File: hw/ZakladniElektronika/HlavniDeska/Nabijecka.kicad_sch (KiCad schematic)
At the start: 1 part

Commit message: WIP
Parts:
- added C146, C147: 47n, Capacitor_SMD:C_0402_1005Metric, symbol Device:C
- added D126: red, LED_SMD:LED_0603_1608Metric, symbol Device:LED
- added L5: 1u, Robotarna_KiCad_Library:SMD,4.2x4.4mm, symbol Device:L
- added R13: 4.7k, Resistor_SMD:R_0201_0603Metric, symbol Device:R
- added R13: 200k, Resistor_SMD:R_0402_1005Metric, symbol Device:R
- added R13: 10k, Resistor_SMD:R_0402_1005Metric, symbol Device:R
- added R13: 3k, Resistor_SMD:R_0402_1005Metric, symbol Device:R
- added R13: 47k, Resistor_SMD:R_0402_1005Metric, symbol Device:R
- added R13: 15k, Resistor_SMD:R_0402_1005Metric, symbol Device:R
- added R22, R23: 100, Resistor_SMD:R_0402_1005Metric, symbol Device:R
- added U5 (x12): 10uf, Capacitor_SMD:C_0805_2012Metric, symbol B.B-rescue:C-Device-B.B-rescue-B.B-rescue
- added U5: 1n, Capacitor_SMD:C_0402_1005Metric, symbol B.B-rescue:C-Device-B.B-rescue-B.B-rescue
- added U6 (x3): 100n, Capacitor_SMD:C_0402_1005Metric, symbol B.B-rescue:C-Device-B.B-rescue-B.B-rescue
- U35: value ~ -> BQ24179
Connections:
- net GMD: now also U35.G2 (ACDRV2), U35.H2 (ACDRV1), R13.1, R13.1, R13.1, R23.2, U5.2, U5.2, U5.2, U5.2, U5.2, U5.2, U5.2, U5.2, U5.2, U5.2, U5.2, U5.2, U5.2, U6.2, U6.2, U6.2
- net PMID: now also U5.1, U5.1, U5.1, U6.1
- net SW1: now also C147.1, L5.2
- net SW2: now also C146.1, L5.1
- net VBUS: now also U35.G1 (VAC2), U35.H1 (VAC1), U5.1, U5.1, U6.1
- net at U35.A6 (SYS), U35.B6 (SYS), U35.C6 (SYS)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: now also U5.1, U5.1, U5.1, U5.1, U5.1, U6.1
- net BAT: now reaches U35.A7 (BAT), U35.B7 (BAT), U35.C7 (BAT), U35.D7 (BAT), U35.E7 (BAT)
- net BAT: now also R22.2, U5.1, U5.1
- net at U35.D1 (BTST1): now also C147.2
- net at U35.E1 (REGN): now also R13.1
- net at U35.F1 (STAT): now also D126.2 (A)
- net D+: now reaches U35.F2 (D+)
- net D-: now reaches U35.F3 (D-)
- net at U35.F4 (ILIM_HIZ): now also R13.2
- net at U35.F5 (PROG): now also R13.2
- net at U35.F6 (SDRV): now also U5.1
- net at U35.F7 (BTST2): now also C146.2
- net QON: now reaches U35.G3 (QON)
- net CE: now reaches U35.G4 (CE)
- net INT: now reaches U35.G5 (INT)
- net at U35.G6 (BATN): now also R23.1
- net at U35.G7 (BATP): now also R22.1
- net SCL: now reaches U35.H4 (SCL)
- net SDA: now reaches U35.H5 (SDA)
- net at U35.H7 (TS): now also R13.2
- new net: D126.1 (K), R13.2
- new net: R13.1, R13.2 (x2)
- no-connect marks 0 -> 2
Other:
- moved on the sheet: U35

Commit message: Zaciame psat
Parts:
- U35: LCSC (none) -> C2879484
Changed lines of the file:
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@@
       (effects (font (size 1.27 1.27)) hide)
     )
-    (property "Datasheet" "" (at 133.35 50.8 0)
+    (property "Datasheet" "https://www.ti.com/lit/ds/symlink/bq24179.pdf?ts=1698854511988&ref_url=https%253A%252F%252Fwww.ti.com%252Fpower-management%252Fbattery-management%252Fcharger-ics%252Fproducts.html" (at 133.35 50.8 0)
       (effects (font (size 1.27 1.27)) hide)
     )
+    (property "LCSC" "C2879484" (at 133.35 50.8 0)
+      (effects (font (size 1.27 1.27)) hide)
+    )

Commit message: USB_multiplexer a přehlednost
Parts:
- removed C146, C147: 47n, Capacitor_SMD:C_0402_1005Metric, symbol Device:C
- removed L5: 1u, Robotarna_KiCad_Library:SMD,4.2x4.4mm, symbol Device:L
- removed R13: 4.7k, Resistor_SMD:R_0201_0603Metric, symbol Device:R
- removed R13: 200k, Resistor_SMD:R_0402_1005Metric, symbol Device:R
- removed R13: 10k, Resistor_SMD:R_0402_1005Metric, symbol Device:R
- removed R13: 3k, Resistor_SMD:R_0402_1005Metric, symbol Device:R
- removed R13: 47k, Resistor_SMD:R_0402_1005Metric, symbol Device:R
- removed R13: 15k, Resistor_SMD:R_0402_1005Metric, symbol Device:R
- removed R22, R23: 100, Resistor_SMD:R_0402_1005Metric, symbol Device:R
- removed U35: BQ24179, symbol Robotarna_KiCad_Library:BQ24179
- removed U5 (x12): 10uf, Capacitor_SMD:C_0805_2012Metric, symbol B.B-rescue:C-Device-B.B-rescue-B.B-rescue
- removed U5: 1n, Capacitor_SMD:C_0402_1005Metric, symbol B.B-rescue:C-Device-B.B-rescue-B.B-rescue
- removed U6 (x3): 100n, Capacitor_SMD:C_0402_1005Metric, symbol B.B-rescue:C-Device-B.B-rescue-B.B-rescue
- added C150: 4.7u, Capacitor_SMD:C_0805_2012Metric, symbol Device:C
- added C165: 47n, Capacitor_SMD:C_0402_1005Metric, symbol Device:C
- added C3: 1u, Capacitor_SMD:C_0402_1005Metric, symbol Device:C
- added L7: L, Inductor_SMD:L_Abracon_ASPI-0630LR, symbol Device:L
- added R13: 4.7k, Resistor_SMD:R_0201_0603Metric, symbol Device:R
- added R13 (x2): 10k, Resistor_SMD:R_0402_1005Metric, symbol Device:R
- added R17 (x2): 0, Resistor_SMD:R_0805_2012Metric_Pad1.20x1.40mm_HandSolder, symbol Device:R
- added R72: 100, Resistor_SMD:R_0402_1005Metric, symbol Device:R
- added TP4: TestPoint-Charger_QON, symbol Connector:TestPoint
- added TP4: TestPoint-Charger_ILIM, symbol Connector:TestPoint
- added U5 (x3): 10uf, Capacitor_SMD:C_0805_2012Metric, symbol B.B-rescue:C-Device-B.B-rescue-B.B-rescue
- added U9: BQ25895RTW, Package_DFN_QFN:Texas_S-PWQFN-N24_EP2.7x2.7mm_ThermalVias, symbol Battery_Management:BQ25895RTW
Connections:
- net D+: now also U9.2 (D+)
- net D-: now also U9.3 (D-)
- net INT: now also U9.7 (INT)
- net SCL: now also U9.5 (SCL)
- net SDA: now also U9.6 (SDA)
- net VBUS: now also C3.1, U9.1 (VBUS)
- net at D126.1 (K): now also R13.2
- net at D126.2 (A): now also U9.13 (BAT), U9.14 (BAT)
- new net: U5.1, U9.23 (PMID)
- new net: C165.1, L7.1, U9.19 (SW), U9.20 (SW)
- new net: C165.2, U9.21 (BTST)
- new net: C150.1, R13.2, U9.22 (REGN)
- new net: L7.2, U5.1, U5.1, U9.15 (SYS), U9.16 (SYS)
- new net: TP4.1, U9.12 (~{QON})
- new net: R17.2, U9.8 (OTG)
- new net: R17.2, U9.9 (~{CE})
- new net: R72.1, TP4.1, U9.10 (ILIM)
- new net: R13.1, U9.4 (STAT)
- new net: R13.1, R13.1, U9.11 (TS)
- new net DSEL: U9.24 (DSEL)
- new net GND: C150.2, C3.2, R13.2, R17.1, R17.1, R72.2, U5.2, U5.2, U5.2, U9.17 (PGND), U9.18 (PGND), U9.25 (PGND)
- no-connect marks 2 -> 0

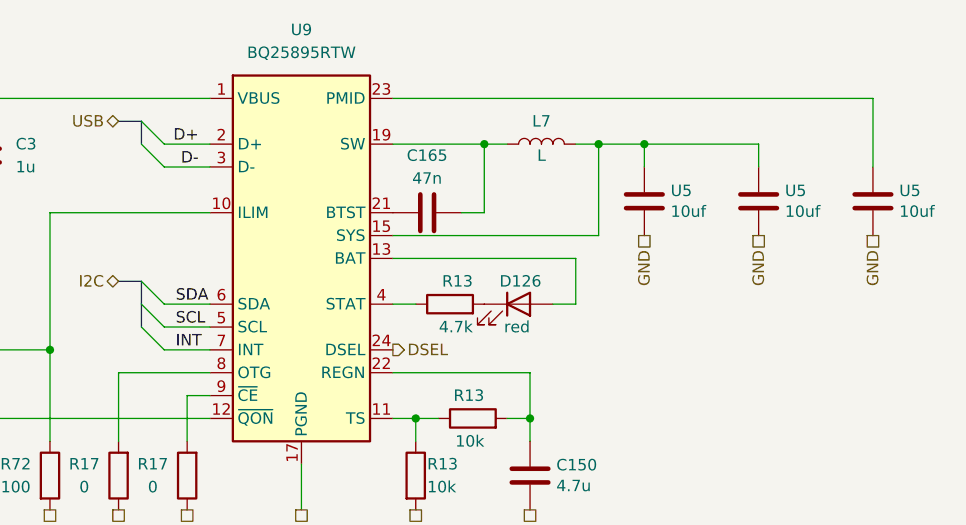
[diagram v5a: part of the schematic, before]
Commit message: Likvidace MiniUI jako samostatné desky a výběr všech komponent
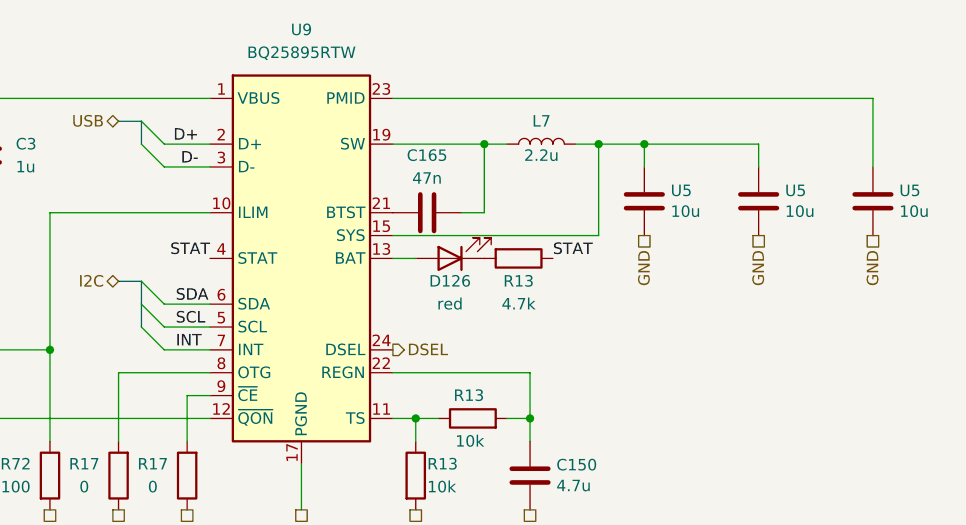
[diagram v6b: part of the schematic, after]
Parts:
- C150: footprint Capacitor_SMD:C_0805_2012Metric -> Capacitor_SMD:C_0603_1608Metric; Basic/Extended (none) -> B; LCSC C1779 -> C19666; info (none) -> 16V, X5R
- C165: footprint Capacitor_SMD:C_0402_1005Metric -> Capacitor_SMD:C_0603_1608Metric; Basic/Extended (none) -> B; LCSC (none) -> C1622; info (none) -> 50V, X7R
- C3: JLCPCB_CORRECTION (none) -> 0;0;0; info 50V, X7R -> 50V, X5R (potenciálně C52923 což je 25V, X5R )
- L7: value L -> 2.2u; Basic/Extended (none) -> E
- R13: footprint Resistor_SMD:R_0201_0603Metric -> Resistor_SMD:R_0402_1005Metric; Basic/Extended E -> B; LCSC C270346 -> C25900
- R13: JLCPCB_CORRECTION (none) -> 0;0;0
- R17: Basic/Extended (none) -> B; LCSC C908865 -> C17477
- R72: Basic/Extended (none) -> B
- TP4: JLCPCB_IGNORE (none) -> ignore
- U5: value 10uf -> 10u; footprint Capacitor_SMD:C_0805_2012Metric -> Capacitor_SMD:C_0603_1608Metric; Basic/Extended (none) -> B; LCSC C15850 -> C96446; info (none) -> 25V, X5R
- U9: Basic/Extended (none) -> E; LCSC (none) -> C80200
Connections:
- net STAT: now reaches R13.1, U9.4 (STAT)
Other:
- moved on the sheet: D126, R13

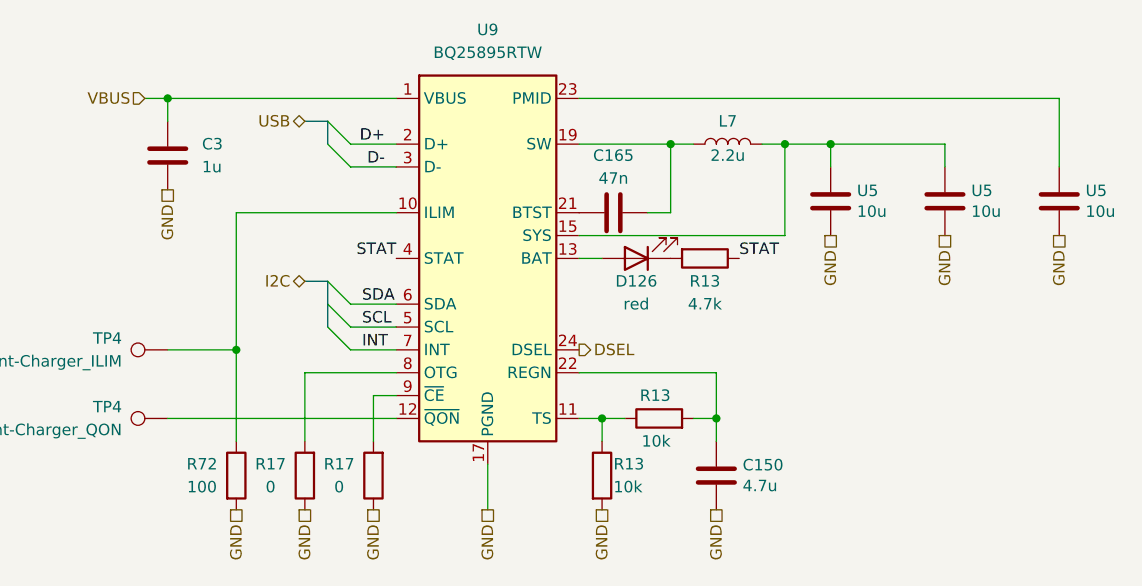
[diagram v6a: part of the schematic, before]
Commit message: Výmněna ochrany baterie
Předchozí ochranný čip JLCPCB nemělo na skladě
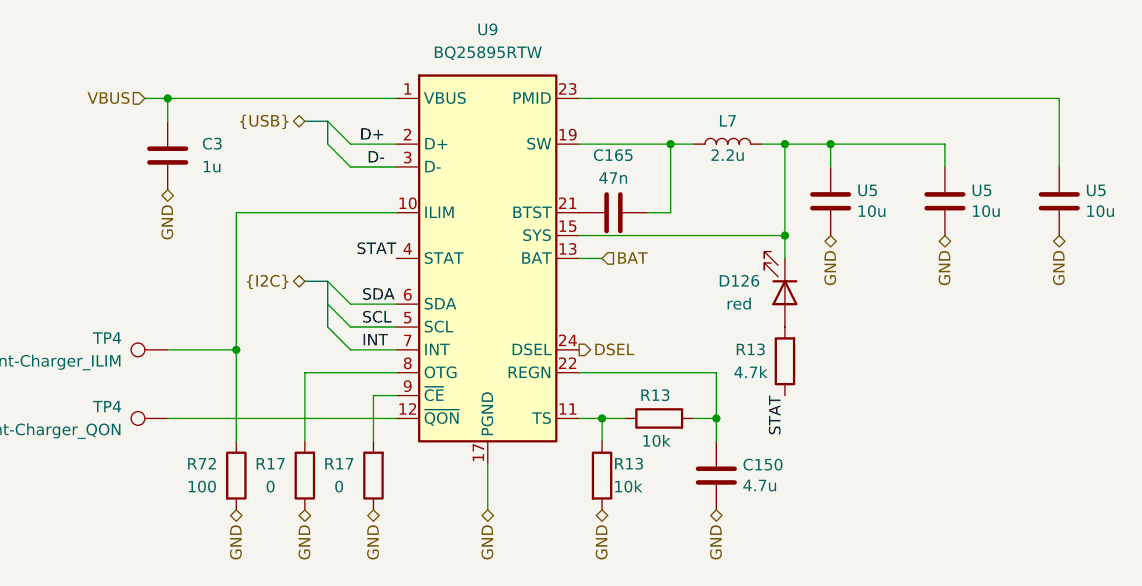
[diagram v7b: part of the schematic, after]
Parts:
- TP4: footprint (none) -> Connector_Pin:Pin_D0.9mm_L10.0mm_W2.4mm_FlatFork
- U5: symbol B.B-rescue:C-Device-B.B-rescue-B.B-rescue -> Device:C
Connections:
- net at L7.2, U5.1, U5.1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: now also D126.1 (K)
- net at R13.2: now also D126.2 (A); no longer D126.1 (K)
- net BAT: now reaches U9.13 (BAT), U9.14 (BAT)
- net BAT: no longer D126.2 (A)
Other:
- moved on the sheet: D126, R13
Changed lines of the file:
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@@
   (junction (at 109.22 91.44) (diameter 0) (color 0 0 0 0)
   )
+  (junction (at 170.18 78.74) (diameter 0) (color 0 0 0 0)
+  )
   (junction (at 101.6 63.5) (diameter 0) (color 0 0 0 0)
   )
@@
   )
   (wire (pts (xy 170.18 78.74) (xy 170.18 68.58))
+    (stroke (width 0) (type default))
+  )
+  (wire (pts (xy 170.18 78.74) (xy 170.18 81.28))
     (stroke (width 0) (type default))
   )
@@
     (effects (font (size 1.27 1.27)) (justify left bottom))
   )
-  (label "STAT" (at 165.1 81.28 0) (fields_autoplaced)
-    (effects (font (size 1.27 1.27)) (justify left bottom))
+  (label "STAT" (at 170.18 96.52 270) (fields_autoplaced)
+    (effects (font (size 1.27 1.27)) (justify right bottom))
   )
   (hierarchical_label "VBUS" (shape input) (at 99.06 63.5 180) (fields_autoplaced)
@@
     (effects (font (size 1.27 1.27)) (justify left))
   )
-  (hierarchical_label "GND" (shape passive) (at 109.22 109.22 270) (fields_autoplaced)
-    (effects (font (size 1.27 1.27)) (justify right))
-  )
-  (hierarchical_label "GND" (shape passive) (at 187.96 78.74 270) (fields_autoplaced)
-    (effects (font (size 1.27 1.27)) (justify right))
-  )
-  (hierarchical_label "GND" (shape passive) (at 101.6 73.66 270) (fields_autoplaced)
-    (effects (font (size 1.27 1.27)) (justify right))
-  )
-  (hierarchical_label "GND" (shape passive) (at 162.56 109.22 270) (fields_autoplaced)
-    (effects (font (size 1.27 1.27)) (justify right))
-  )
-  (hierarchical_label "I2C" (shape bidirectional) (at 116.84 83.82 180) (fields_autoplaced)
-    (effects (font (size 1.27 1.27)) (justify right))
-  )
-  (hierarchical_label "USB" (shape bidirectional) (at 116.84 66.04 180) (fields_autoplaced)
-    (effects (font (size 1.27 1.27)) (justify right))
-  )
-  (hierarchical_label "GND" (shape passive) (at 149.86 109.22 270) (fields_autoplaced)
-    (effects (font (size 1.27 1.27)) (justify right))
-  )
-  (hierarchical_label "GND" (shape passive) (at 175.26 78.74 270) (fields_autoplaced)
-    (effects (font (size 1.27 1.27)) (justify right))
-  )
-  (hierarchical_label "GND" (shape passive) (at 200.66 78.74 270) (fields_autoplaced)
-    (effects (font (size 1.27 1.27)) (justify right))
-  )
-  (hierarchical_label "GND" (shape passive) (at 124.46 109.22 270) (fields_autoplaced)
-    (effects (font (size 1.27 1.27)) (justify right))
-  )
-  (hierarchical_label "GND" (shape passive) (at 137.16 109.22 270) (fields_autoplaced)
-    (effects (font (size 1.27 1.27)) (justify right))
-  )
-  (hierarchical_label "GND" (shape passive) (at 116.84 109.22 270) (fields_autoplaced)
-    (effects (font (size 1.27 1.27)) (justify right))
-  )
-  (symbol (lib_id "B.B-rescue:C-Device-B.B-rescue-B.B-rescue") (at 200.66 74.93 0) (unit 1)
+  (hierarchical_label "BAT" (shape input) (at 149.86 81.28 0) (fields_autoplaced)
+    (effects (font (size 1.27 1.27)) (justify left))
+  )
+  (hierarchical_label "GND" (shape bidirectional) (at 109.22 109.22 270) (fields_autoplaced)
+    (effects (font (size 1.27 1.27)) (justify right))
+  )
+  (hierarchical_label "GND" (shape bidirectional) (at 187.96 78.74 270) (fields_autoplaced)
+    (effects (font (size 1.27 1.27)) (justify right))
+  )
+  (hierarchical_label "GND" (shape bidirectional) (at 101.6 73.66 270) (fields_autoplaced)
+    (effects (font (size 1.27 1.27)) (justify right))
+  )
+  (hierarchical_label "GND" (shape bidirectional) (at 162.56 109.22 270) (fields_autoplaced)
+    (effects (font (size 1.27 1.27)) (justify right))
+  )
+  (hierarchical_label "{I2C}" (shape bidirectional) (at 116.84 83.82 180) (fields_autoplaced)
+    (effects (font (size 1.27 1.27)) (justify right))
+  )
+  (hierarchical_label "{USB}" (shape bidirectional) (at 116.84 66.04 180) (fields_autoplaced)
+    (effects (font (size 1.27 1.27)) (justify right))
+  )
+  (hierarchical_label "GND" (shape bidirectional) (at 149.86 109.22 270) (fields_autoplaced)
+    (effects (font (size 1.27 1.27)) (justify right))
+  )
+  (hierarchical_label "GND" (shape bidirectional) (at 175.26 78.74 270) (fields_autoplaced)
+    (effects (font (size 1.27 1.27)) (justify right))
+  )
+  (hierarchical_label "GND" (shape bidirectional) (at 200.66 78.74 270) (fields_autoplaced)
+    (effects (font (size 1.27 1.27)) (justify right))
+  )
+  (hierarchical_label "GND" (shape bidirectional) (at 124.46 109.22 270) (fields_autoplaced)
+    (effects (font (size 1.27 1.27)) (justify right))
+  )
+  (hierarchical_label "GND" (shape bidirectional) (at 137.16 109.22 270) (fields_autoplaced)
+    (effects (font (size 1.27 1.27)) (justify right))
+  )
+  (hierarchical_label "GND" (shape bidirectional) (at 116.84 109.22 270) (fields_autoplaced)
+    (effects (font (size 1.27 1.27)) (justify right))
+  )
+  (symbol (lib_id "Device:C") (at 200.66 74.93 0) (unit 1)
     (in_bom yes) (on_board yes) (dnp no)
     (property "Reference" "U5" (at 203.581 73.7616 0)
@@
     )
   )
-  (symbol (lib_id "B.B-rescue:C-Device-B.B-rescue-B.B-rescue") (at 187.96 74.93 0) (unit 1)
+  (symbol (lib_id "Device:C") (at 187.96 74.93 0) (unit 1)
     (in_bom yes) (on_board yes) (dnp no)
     (property "Reference" "U5" (at 190.881 73.7616 0)
@@
       (effects (font (size 1.27 1.27)) (justify left))
     )
-    (property "Footprint" "" (at 101.6 93.98 0)
+    (property "Footprint" "Connector_Pin:Pin_D0.9mm_L10.0mm_W2.4mm_FlatFork" (at 101.6 93.98 0)
       (effects (font (size 1.27 1.27)) hide)
     )
@@
       (effects (font (size 1.27 1.27)) (justify left))
     )
-    (property "Footprint" "" (at 101.6 86.36 0)
+    (property "Footprint" "Connector_Pin:Pin_D0.9mm_L10.0mm_W2.4mm_FlatFork" (at 101.6 86.36 0)
       (effects (font (size 1.27 1.27)) hide)
     )
@@
     )
   )
-  (symbol (lib_id "Device:R") (at 161.29 81.28 270) (unit 1)
-    (in_bom yes) (on_board yes) (dnp no)
-    (property "Reference" "R13" (at 161.29 83.82 90)
-      (effects (font (size 1.27 1.27)))
-    )
-    (property "Value" "4.7k" (at 161.29 86.36 90)
-      (effects (font (size 1.27 1.27)))
-    )
-    (property "Footprint" "Resistor_SMD:R_0402_1005Metric" (at 161.29 79.502 90)
-      (effects (font (size 1.27 1.27)) hide)
-    )
-    (property "Datasheet" "~" (at 161.29 81.28 0)
-      (effects (font (size 1.27 1.27)) hide)
-    )
-    (property "LCSC" "C25900" (at 161.29 81.28 0)
-      (effects (font (size 1.27 1.27)) hide)
-    )
-    (property "Basic/Extended" "B" (at 161.29 81.28 0)
+  (symbol (lib_id "Device:R") (at 170.18 92.71 180) (unit 1)
+    (in_bom yes) (on_board yes) (dnp no)
+    (property "Reference" "R13" (at 166.37 91.44 0)
+      (effects (font (size 1.27 1.27)))
+    )
+    (property "Value" "4.7k" (at 166.37 93.98 0)
+      (effects (font (size 1.27 1.27)))
+    )
+    (property "Footprint" "Resistor_SMD:R_0402_1005Metric" (at 171.958 92.71 90)
+      (effects (font (size 1.27 1.27)) hide)
+    )
+    (property "Datasheet" "~" (at 170.18 92.71 0)
+      (effects (font (size 1.27 1.27)) hide)
+    )
+    (property "LCSC" "C25900" (at 170.18 92.71 0)
+      (effects (font (size 1.27 1.27)) hide)
+    )
+    (property "Basic/Extended" "B" (at 170.18 92.71 0)
       (effects (font (size 1.27 1.27)) hide)
     )
@@
     )
   )
-  (symbol (lib_id "B.B-rescue:C-Device-B.B-rescue-B.B-rescue") (at 175.26 74.93 0) (unit 1)
+  (symbol (lib_id "Device:C") (at 175.26 74.93 0) (unit 1)
     (in_bom yes) (on_board yes) (dnp no)
     (property "Reference" "U5" (at 178.181 73.7616 0)
@@
     )
   )
-  (symbol (lib_id "Device:LED") (at 153.67 81.28 180) (unit 1)
-    (in_bom yes) (on_board yes) (dnp no)
-    (property "Reference" "D126" (at 153.67 83.82 0)
-      (effects (font (size 1.27 1.27)))
-    )
-    (property "Value" "red" (at 153.67 86.36 0)
-      (effects (font (size 1.27 1.27)))
-    )
-    (property "Footprint" "LED_SMD:LED_0603_1608Metric" (at 153.67 81.28 0)
-      (effects (font (size 1.27 1.27)) hide)
-    )
-    (property "Datasheet" "~" (at 153.67 81.28 0)
-      (effects (font (size 1.27 1.27)) hide)
-    )
-    (property "LCSC" "C2286" (at 153.67 81.28 90)
-      (effects (font (size 1.27 1.27)) hide)
-    )
-    (property "Basic/Extended" "B" (at 153.67 81.28 90)
+  (symbol (lib_id "Device:LED") (at 170.18 85.09 270) (unit 1)
+    (in_bom yes) (on_board yes) (dnp no)
+    (property "Reference" "D126" (at 165.1 83.82 90)
+      (effects (font (size 1.27 1.27)))
+    )
+    (property "Value" "red" (at 165.1 86.36 90)
+      (effects (font (size 1.27 1.27)))
+    )
+    (property "Footprint" "LED_SMD:LED_0603_1608Metric" (at 170.18 85.09 0)
+      (effects (font (size 1.27 1.27)) hide)
+    )
+    (property "Datasheet" "~" (at 170.18 85.09 0)
+      (effects (font (size 1.27 1.27)) hide)
+    )
+    (property "LCSC" "C2286" (at 170.18 85.09 90)
+      (effects (font (size 1.27 1.27)) hide)
+    )
+    (property "Basic/Extended" "B" (at 170.18 85.09 90)
       (effects (font (size 1.27 1.27)) hide)
     )
@@
         )
         (path "/99cd3e15-4eb6-4cbb-8726-789aedd3df15/c3b70d9b-0dcb-4344-9507-13ff5b4c000e/aae02708-da26-44dd-a602-660fbe003309/4ff5c299-eafc-48ae-8fce-c1c1f5f569e7"
-          (reference "LED") (unit 1)
-        )
-      )
+          (reference "LED5") (unit 1)
+        )
+      )

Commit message: PCB
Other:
- moved on the sheet: C150, C165, D126, L7, R13, R17, R72, U5, U9
